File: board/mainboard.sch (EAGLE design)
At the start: 3 parts

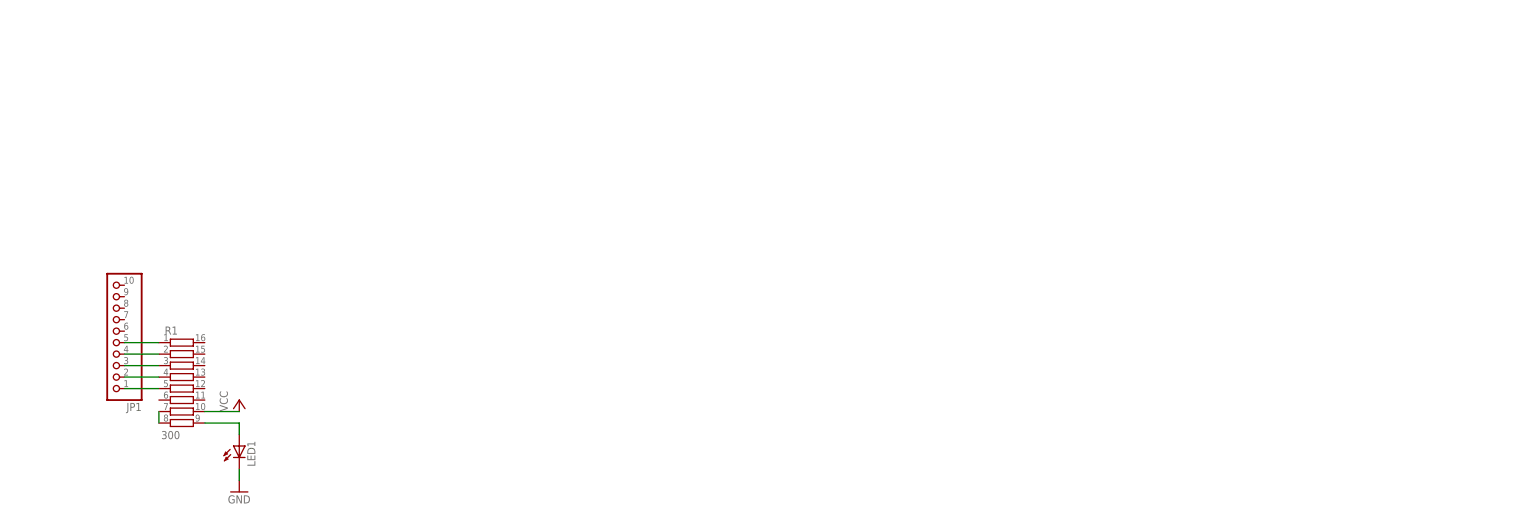
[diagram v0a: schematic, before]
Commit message: board: add more components into mainboard
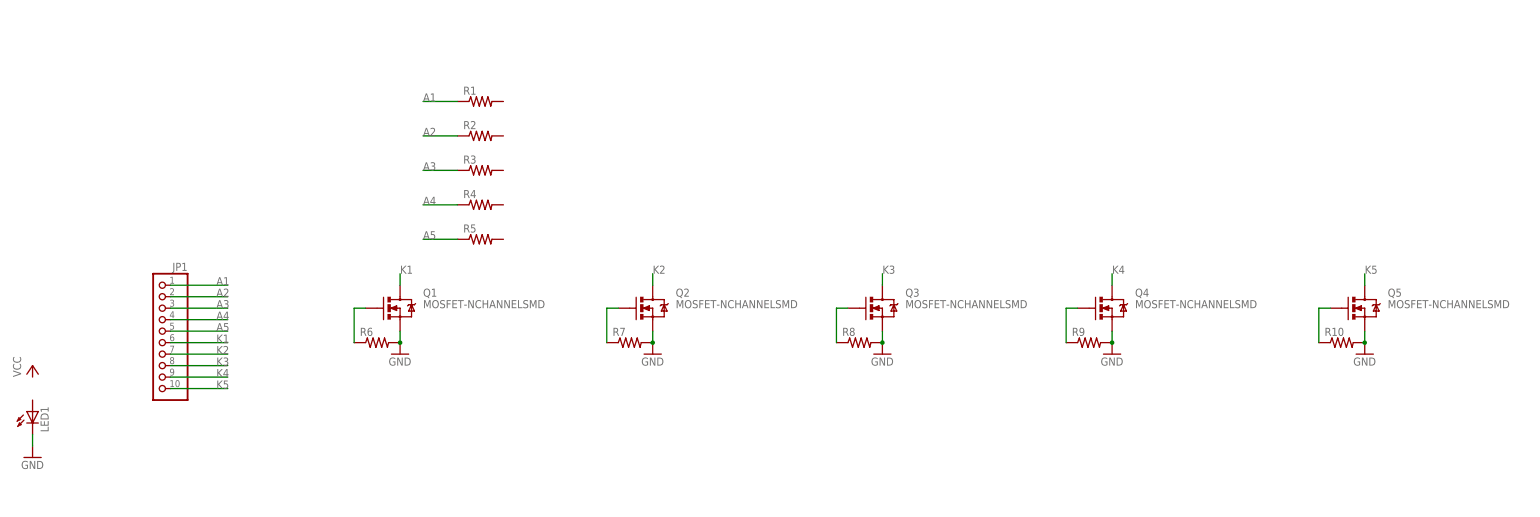
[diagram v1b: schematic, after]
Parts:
- added Q1, Q2, Q3, Q4, Q5: MOSFET-NCHANNELSMD, SparkFun:MOSFET-NCHANNELSMD
- added R10, R2, R3, R4, R5, R6, R7, R8, R9: (no value), rcl:R-US_M1206
- R1: value 300 -> (none); device resistor-bourns:2QSP16-8 -> rcl:R-US_M1206
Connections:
- removed net N$6: R1.7, R1.8
- removed net N$7: LED1.A, R1.9
- removed net VCC: R1.10
- new net A1: JP1.1, R1.1
- new net A2: JP1.2, R2.1
- new net A3: JP1.3, R3.1
- new net A4: JP1.4, R4.1
- new net A5: JP1.5, R5.1
- new net K1: JP1.6, Q1.D
- new net K2: JP1.7, Q2.D
- new net K3: JP1.8, Q3.D
- new net K4: JP1.9, Q4.D
- new net K5: JP1.10, Q5.D
- net GND: now also Q1.S, Q2.S, Q3.S, Q4.S, Q5.S, R10.2, R6.2, R7.2, R8.2, R9.2
- net N$1: now also Q1.G, R6.1; no longer JP1.5, R1.1
- net N$2: now also Q2.G, R7.1; no longer JP1.4, R1.2
- net N$3: now also Q3.G, R8.1; no longer JP1.3, R1.3
- net N$4: now also Q4.G, R9.1; no longer JP1.2, R1.4
- net N$5: now also Q5.G, R10.1; no longer JP1.1, R1.5
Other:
- moved on the sheet: JP1, LED1

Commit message: board: add arduino to mainboard
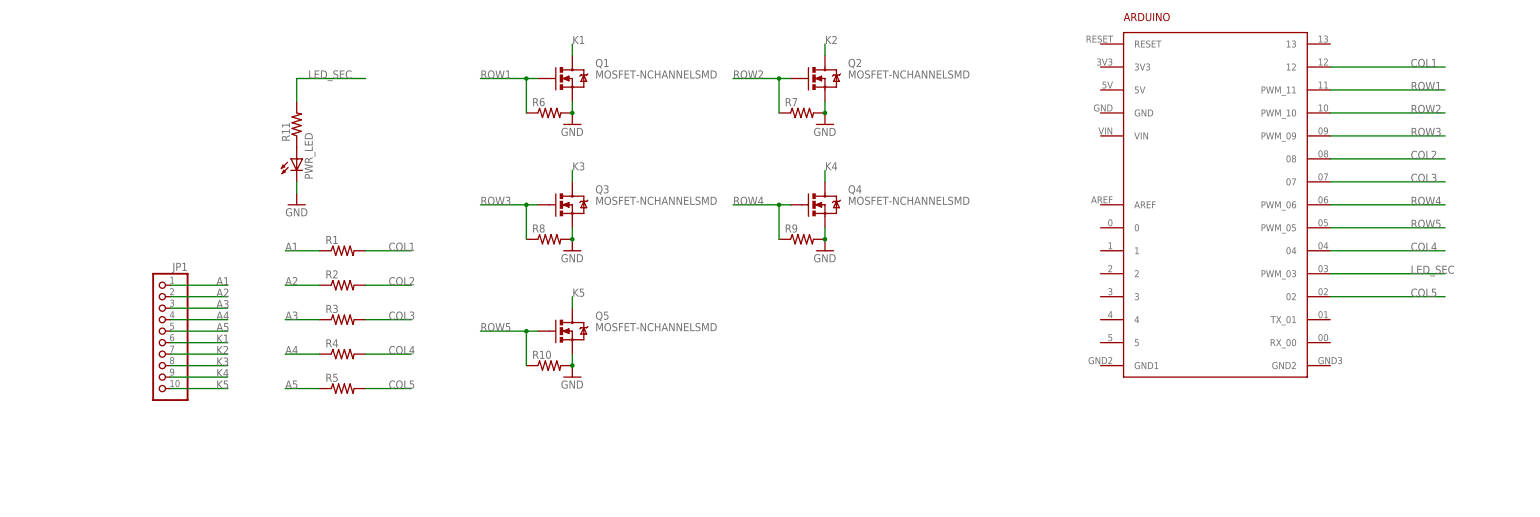
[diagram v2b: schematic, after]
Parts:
- removed LED1: (no value), led:LED5MM
- added ARDUINO1: ARDUINO, arduino:ARDUINO
- added PWR_LED: (no value), led:LED5MM
- added R11: (no value), rcl:R-US_M1206
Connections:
- removed net N$2: Q2.G, R7.1
- removed net N$3: Q3.G, R8.1
- removed net N$4: Q4.G, R9.1
- removed net N$5: Q5.G, R10.1
- new net COL1: ARDUINO1.12, R1.2
- new net COL2: ARDUINO1.08, R2.2
- new net COL3: ARDUINO1.07, R3.2
- new net COL4: ARDUINO1.04, R4.2
- new net COL5: ARDUINO1.02, R5.2
- new net LED_SEC: ARDUINO1.PWM_03, R11.2
- new net ROW1: ARDUINO1.PWM_11, Q1.G, R6.1
- new net ROW2: ARDUINO1.PWM_10, Q2.G, R7.1
- new net ROW3: ARDUINO1.PWM_09, Q3.G, R8.1
- new net ROW4: ARDUINO1.PWM_06, Q4.G, R9.1
- new net ROW5: ARDUINO1.PWM_05, Q5.G, R10.1
- net GND: now also PWR_LED.C; no longer LED1.C
- net N$1: now also PWR_LED.A, R11.1; no longer Q1.G, R6.1
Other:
- moved on the sheet: Q1, Q2, Q3, Q4, Q5, R1, R10, R2, R3, R4, R5, R6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
